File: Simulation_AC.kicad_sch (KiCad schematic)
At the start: 2 parts

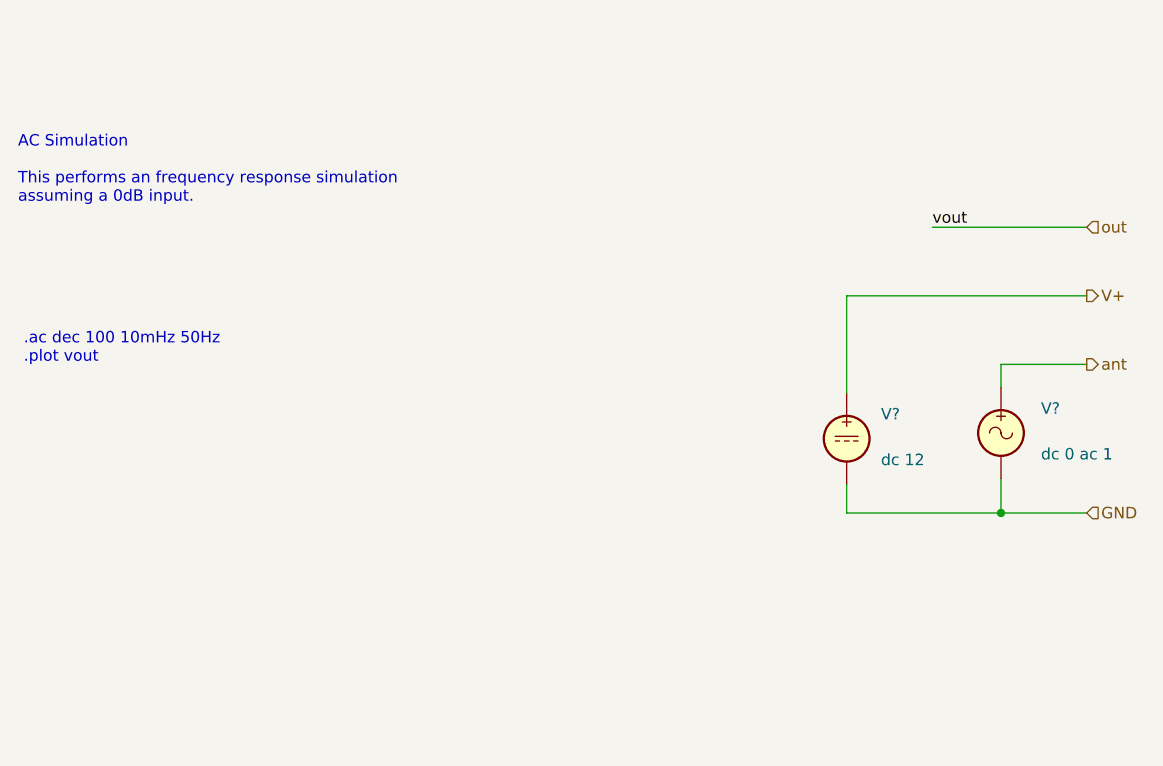
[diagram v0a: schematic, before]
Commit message: Fix simulation primitives and document simulation types
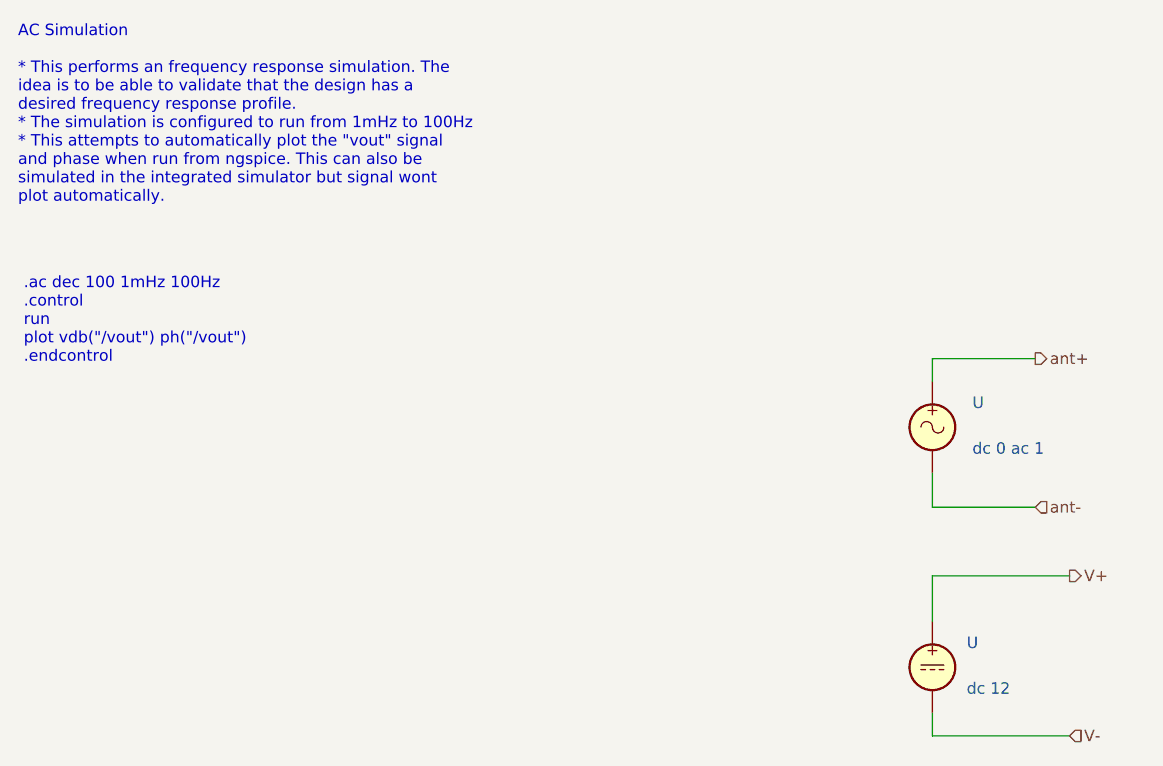
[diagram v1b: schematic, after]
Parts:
- U: renamed from V?; value ~ -> (none)
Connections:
- net GND renamed V-
- net V-: no longer U.2
- net ant renamed ant+
- new net ant-: U.2
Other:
- note added: ".ac dec 100 1mHz 100Hz .control run plot vdb("/vout") ph("/vout") .endcontrol"
- note added: "AC Simulation * This performs an frequency response simulation. The idea is to be able to validate that the design has a desired frequency response profile. * The simulation is configured to run from 1mHz to 100Hz * This attempts to automatically plot the "vout" signal and phase when run from ngspice. This can also be simulated in the integrated simulator but signal wont plot automatically."
- note removed: ".ac dec 100 10mHz 50Hz .plot vout"
- note removed: "AC Simulation This performs an frequency response simulation assuming a 0dB input."
- moved on the sheet: U
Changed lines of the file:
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@@
-(kicad_sch (version 20211123) (generator eeschema)
+(kicad_sch (version 20220404) (generator eeschema)
   (paper "A4")
-  (junction (at 172.72 89.535) (diameter 0) (color 0 0 0 0)
+  (wire (pts (xy 165.1 88.9) (xy 165.1 85.09))
+    (stroke (width 0) (type default))
   )
-  (wire (pts (xy 155.575 86.36) (xy 155.575 89.535))
-    (stroke (width 0) (type default) (color 0 0 0 0))
+  (wire (pts (xy 180.34 96.52) (xy 165.1 96.52))
+    (stroke (width 0) (type default))
   )
-  (wire (pts (xy 172.72 75.565) (xy 172.72 73.025))
-    (stroke (width 0) (type default) (color 0 0 0 0))
+  (wire (pts (xy 180.34 114.3) (xy 165.1 114.3))
+    (stroke (width 0) (type default))
   )
-  (wire (pts (xy 172.72 73.025) (xy 182.245 73.025))
-    (stroke (width 0) (type default) (color 0 0 0 0))
+  (wire (pts (xy 165.1 114.3) (xy 165.1 111.76))
+    (stroke (width 0) (type default))
   )
-  (wire (pts (xy 182.245 89.535) (xy 172.72 89.535))
-    (stroke (width 0) (type default) (color 0 0 0 0))
+  (wire (pts (xy 165.1 96.52) (xy 165.1 101.6))
+    (stroke (width 0) (type default))
   )
-  (wire (pts (xy 155.575 65.405) (xy 182.245 65.405))
-    (stroke (width 0) (type default) (color 0 0 0 0))
+  (wire (pts (xy 176.53 88.9) (xy 165.1 88.9))
+    (stroke (width 0) (type default))
   )
-  (wire (pts (xy 155.575 89.535) (xy 172.72 89.535))
-    (stroke (width 0) (type default) (color 0 0 0 0))
+  (wire (pts (xy 165.1 72.39) (xy 176.53 72.39))
+    (stroke (width 0) (type default))
   )
-  (wire (pts (xy 172.72 85.725) (xy 172.72 89.535))
-    (stroke (width 0) (type default) (color 0 0 0 0))
+  (wire (pts (xy 165.1 74.93) (xy 165.1 72.39))
+    (stroke (width 0) (type default))
   )
-  (wire (pts (xy 165.1 57.785) (xy 182.245 57.785))
-    (stroke (width 0) (type default) (color 0 0 0 0))
-  )
-  (wire (pts (xy 155.575 76.2) (xy 155.575 65.405))
-    (stroke (width 0) (type default) (color 0 0 0 0))
-  )
-  (text "AC Simulation\n\nThis performs an frequency response simulation\nassuming a 0dB input."
+  (text "AC Simulation\n\n* This performs an frequency response simulation. The\nidea is to be able to validate that the design has a\ndesired frequency response profile.\n* The simulation is configured to run from 1mHz to 100Hz\n* This attempts to automatically plot the \"vout\" signal\nand phase when run from ngspice. This can also be\nsimulated in the integrated simulator but signal wont\nplot automatically.\n"
     (at 63.5 55.245 0)
     (effects (font (size 1.27 1.27)) (justify left bottom))
   )
-  (text ".ac dec 100 10mHz 50Hz\n.plot vout" (at 64.135 73.025 0)
+  (text ".ac dec 100 1mHz 100Hz\n.control\nrun\nplot vdb(\"/vout\") ph(\"/vout\")\n.endcontrol"
+    (at 64.135 73.025 0)
     (effects (font (size 1.27 1.27)) (justify left bottom))
   )
-  (label "vout" (at 165.1 57.785 0)
-    (effects (font (size 1.27 1.27)) (justify left bottom))
-  )
-  (hierarchical_label "out" (shape input) (at 182.245 57.785 0)
+  (hierarchical_label "ant-" (shape input) (at 176.53 88.9 0) (fields_autoplaced)
     (effects (font (size 1.27 1.27)) (justify left))
   )
-  (hierarchical_label "GND" (shape input) (at 182.245 89.535 0)
+  (hierarchical_label "V-" (shape input) (at 180.34 114.3 0) (fields_autoplaced)
     (effects (font (size 1.27 1.27)) (justify left))
   )
-  (hierarchical_label "ant" (shape output) (at 182.245 73.025 0)
+  (hierarchical_label "ant+" (shape output) (at 176.53 72.39 0) (fields_autoplaced)
     (effects (font (size 1.27 1.27)) (justify left))
   )
-  (hierarchical_label "V+" (shape output) (at 182.245 65.405 0)
+  (hierarchical_label "V+" (shape output) (at 180.34 96.52 0) (fields_autoplaced)
     (effects (font (size 1.27 1.27)) (justify left))
   )
-  (symbol (lib_id "Simulation_SPICE:VDC") (at 155.575 81.28 0) (unit 1)
+  (symbol (lib_id "Simulation_SPICE:VDC") (at 165.1 106.68 0) (unit 1)
     (in_bom yes) (on_board yes) (fields_autoplaced)
-    (property "Reference" "V?" (id 0) (at 159.385 78.5501 0)
+    (default_instance (reference "U") (unit 1) (value "") (footprint ""))
+    (property "Reference" "U" (id 0) (at 168.91 103.9501 0)
       (effects (font (size 1.27 1.27)) (justify left))
     )
-    (property "Value" "~" (id 1) (at 159.385 81.0901 0)
+    (property "Value" "" (id 1) (at 168.91 106.4901 0)
       (effects (font (size 1.27 1.27)) (justify left))
     )
-    (property "Footprint" "" (id 2) (at 155.575 81.28 0)
+    (property "Footprint" "" (id 2) (at 165.1 106.68 0)
       (effects (font (size 1.27 1.27)) hide)
     )
-    (property "Datasheet" "~" (id 3) (at 155.575 81.28 0)
+    (property "Datasheet" "~" (id 3) (at 165.1 106.68 0)
       (effects (font (size 1.27 1.27)) hide)
     )
-    (property "Spice_Netlist_Enabled" "Y" (id 4) (at 155.575 81.28 0)
+    (property "Spice_Netlist_Enabled" "Y" (id 4) (at 165.1 106.68 0)
       (effects (font (size 1.27 1.27)) (justify left) hide)
     )
-    (property "Spice_Primitive" "V" (id 5) (at 155.575 81.28 0)
+    (property "Spice_Primitive" "V" (id 5) (at 165.1 106.68 0)
       (effects (font (size 1.27 1.27)) (justify left) hide)
     )
-    (property "Spice_Model" "dc 12" (id 6) (at 159.385 83.6301 0)
+    (property "Spice_Model" "dc 12" (id 6) (at 168.91 109.0301 0)
       (effects (font (size 1.27 1.27)) (justify left))
     )
@@
     (pin "2")
   )
-  (symbol (lib_id "Simulation_SPICE:VSIN") (at 172.72 80.645 0) (unit 1)
+  (symbol (lib_id "Simulation_SPICE:VSIN") (at 165.1 80.01 0) (unit 1)
     (in_bom yes) (on_board yes) (fields_autoplaced)
-    (property "Reference" "V?" (id 0) (at 177.165 77.9151 0)
+    (default_instance (reference "U") (unit 1) (value "") (footprint ""))
+    (property "Reference" "U" (id 0) (at 169.545 77.2801 0)
       (effects (font (size 1.27 1.27)) (justify left))
     )
-    (property "Value" "~" (id 1) (at 177.165 80.4551 0)
+    (property "Value" "" (id 1) (at 169.545 79.8201 0)
       (effects (font (size 1.27 1.27)) (justify left))
     )
-    (property "Footprint" "" (id 2) (at 172.72 80.645 0)
+    (property "Footprint" "" (id 2) (at 165.1 80.01 0)
       (effects (font (size 1.27 1.27)) hide)
     )
-    (property "Datasheet" "~" (id 3) (at 172.72 80.645 0)
+    (property "Datasheet" "~" (id 3) (at 165.1 80.01 0)
       (effects (font (size 1.27 1.27)) hide)
     )
-    (property "Spice_Netlist_Enabled" "Y" (id 4) (at 172.72 80.645 0)
+    (property "Spice_Netlist_Enabled" "Y" (id 4) (at 165.1 80.01 0)
       (effects (font (size 1.27 1.27)) (justify left) hide)
     )
-    (property "Spice_Primitive" "V" (id 5) (at 172.72 80.645 0)
+    (property "Spice_Primitive" "V" (id 5) (at 165.1 80.01 0)
       (effects (font (size 1.27 1.27)) (justify left) hide)
     )
-    (property "Spice_Model" "dc 0 ac 1" (id 6) (at 177.165 82.9951 0)
+    (property "Spice_Model" "dc 0 ac 1" (id 6) (at 169.545 82.3601 0)
       (effects (font (size 1.27 1.27)) (justify left))
     )
